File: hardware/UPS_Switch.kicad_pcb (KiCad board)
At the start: 2 copper layers, 28 parts, among them J1 Screw_Terminal_01x04, J3 Screw_Terminal_01x06, J4 Screw_Terminal_01x06, U1 ESP32-DEVKIT-V1, U2 TPS259807ONRGER, U3 TPS259807ONRGER, U4 TPS259807ONRGER

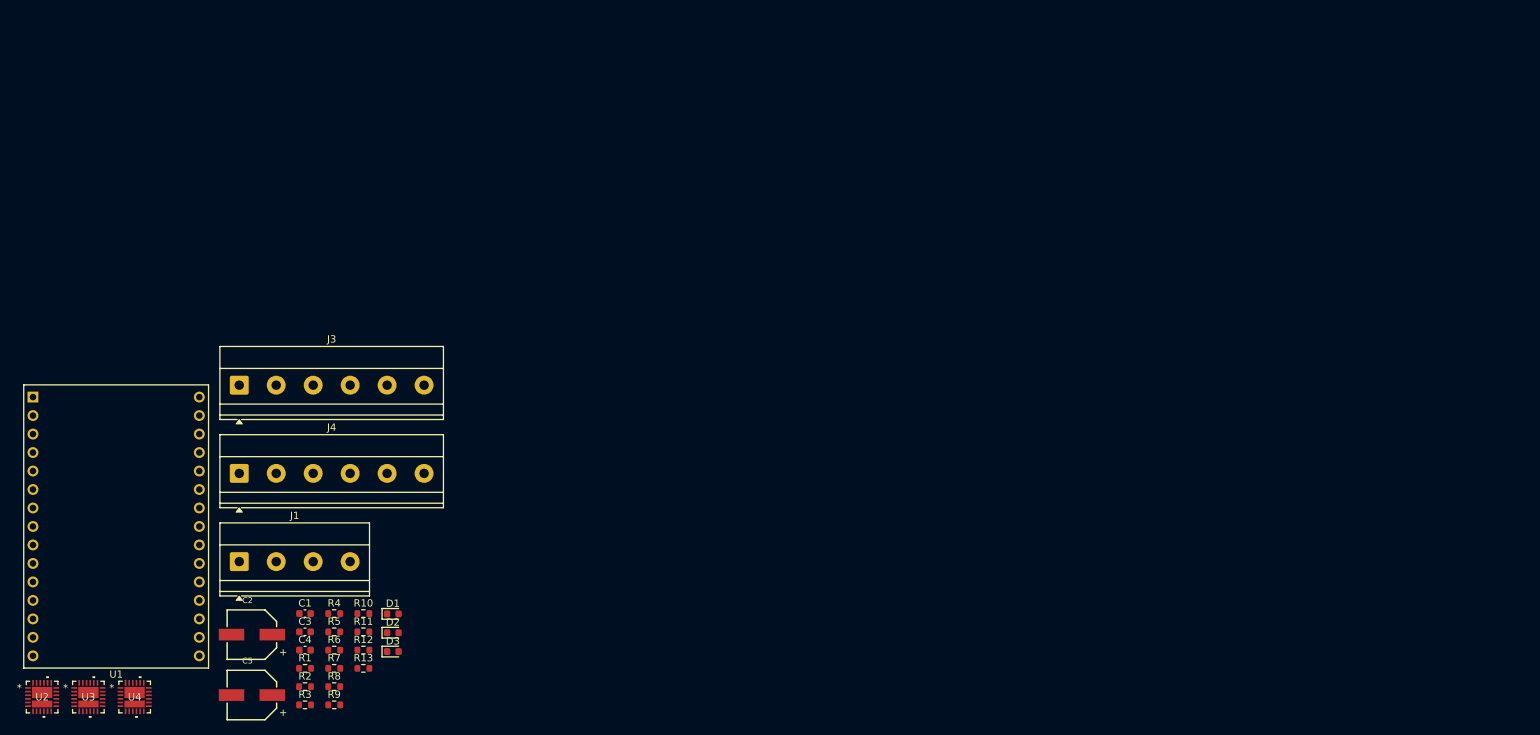
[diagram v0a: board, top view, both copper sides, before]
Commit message: layout fixes
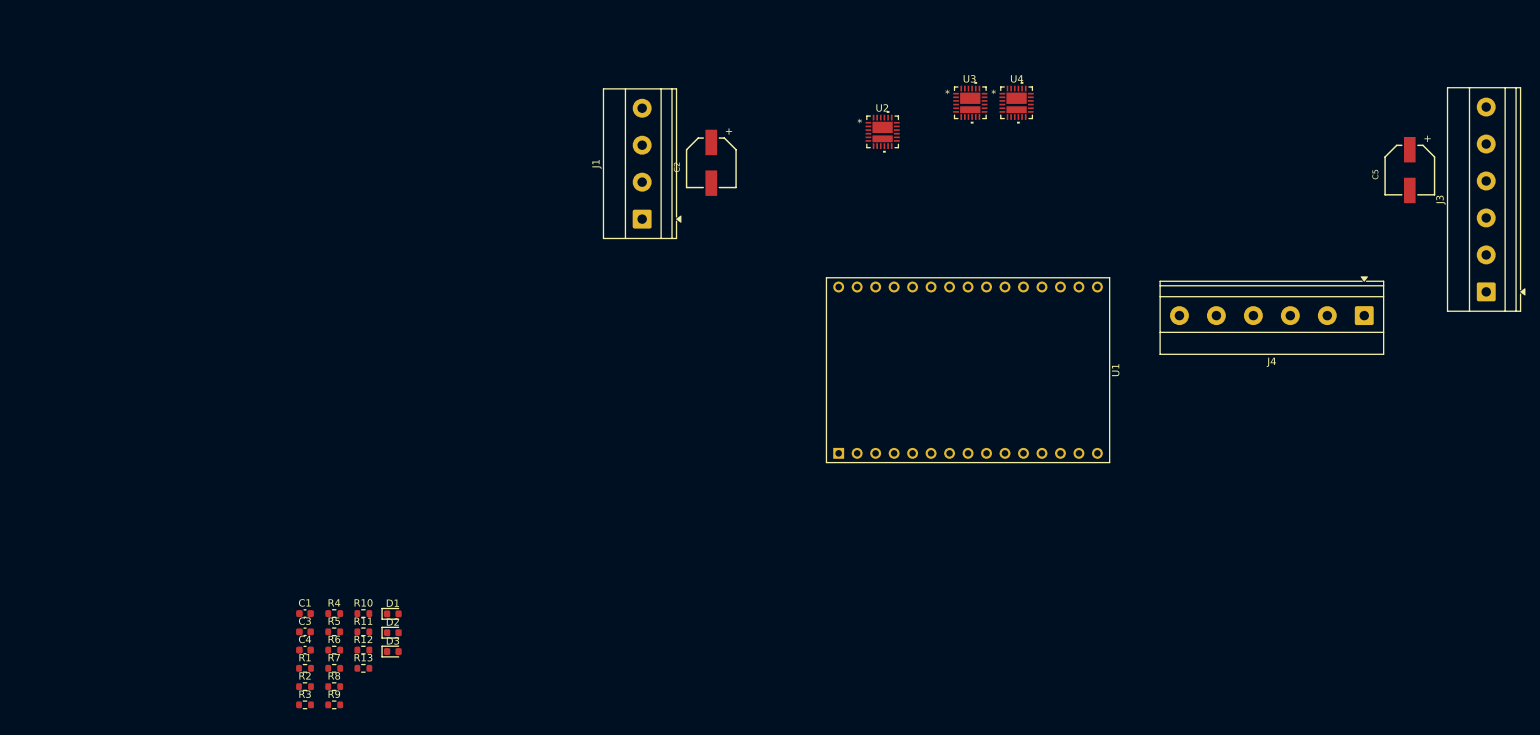
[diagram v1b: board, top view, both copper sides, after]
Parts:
- moved C5 174.7 mm to (130.0, 37.5), turned to 90 degrees
- moved J3 171.9 mm to (140.5, 54.2), turned to 90 degrees
- moved J4 156.1 mm to (123.7, 57.5), turned to 180 degrees
- moved U3 146.2 mm to (69.6, 28.2)
- moved U4 146.2 mm to (76.0, 28.2)
- moved U2 139.2 mm to (57.5, 32.2)
- moved U1 111.0 mm to (51.5, 76.4), turned to 90 degrees
- moved C2 90.5 mm to (34.0, 36.5), turned to 90 degrees
- moved J1 72.7 mm to (24.5, 44.2), turned to 90 degrees

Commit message: Updated layout and screengrabs
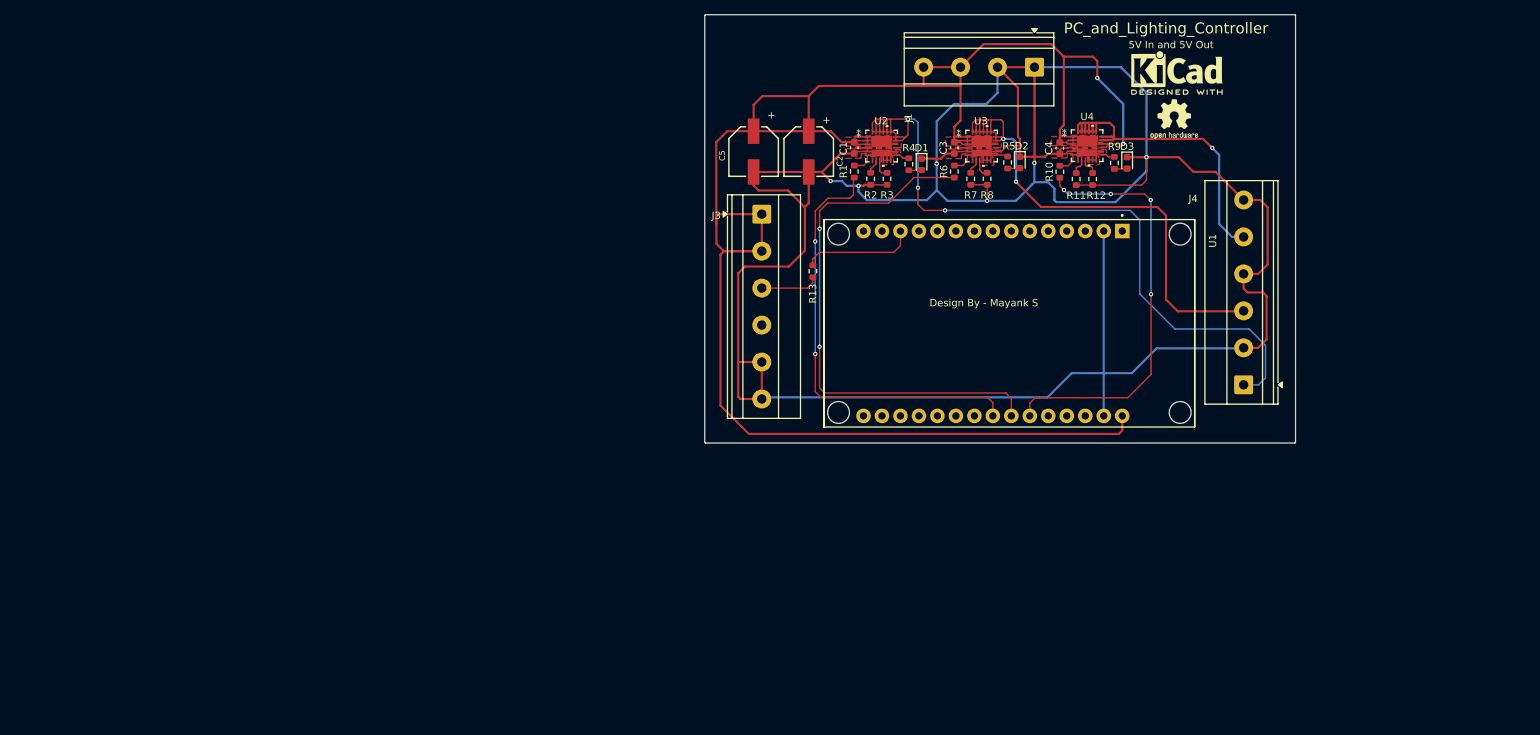
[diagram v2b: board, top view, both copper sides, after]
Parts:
- added REF**: KiCad-Logo2_5mm_SilkScreen, Symbol:KiCad-Logo2_5mm_SilkScreen, F.Cu at (98.0, 24.1)
- added REF**: OSHW-Logo2_7.3x6mm_SilkScreen, Symbol:OSHW-Logo2_7.3x6mm_SilkScreen, F.Cu at (97.6, 30.5)
- U1: footprint RF_Module:ESP32-C3-DevKitM-1 -> Footprints:MODULE_ESP32_DEVKIT_V1
- moved R9 130.6 mm to (89.4, 36.5), turned to 90 degrees
- moved C4 124.6 mm to (81.9, 34.5), turned to -90 degrees
- moved D3 121.2 mm to (91.2, 36.5), turned to -90 degrees
- moved R12 119.3 mm to (86.4, 38.7), turned to -90 degrees
- moved R11 116.1 mm to (84.2, 38.7), turned to -90 degrees
- moved R8 113.7 mm to (71.9, 38.7), turned to -90 degrees
- moved R10 113.3 mm to (81.9, 37.7), turned to 90 degrees
- moved R5 112.8 mm to (74.7, 36.4), turned to 90 degrees
- moved C3 111.3 mm to (67.4, 34.4), turned to -90 degrees
- moved R7 110.4 mm to (69.7, 38.7), turned to -90 degrees
- moved R3 107.8 mm to (58.1, 38.7), turned to -90 degrees
- moved D2 107.7 mm to (76.4, 36.4), turned to -90 degrees
- moved R6 107.7 mm to (67.4, 37.7), turned to 90 degrees
- moved R2 104.5 mm to (55.9, 38.7), turned to -90 degrees
- moved R1 101.8 mm to (53.6, 37.7), turned to 90 degrees
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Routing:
- net GND: track 0.00 -> 454.6 mm, vias 0 -> 6
- net +5V: track 0.00 -> 290.6 mm, vias 0 -> 2
- net /LED_1_VOUT: track 0.00 -> 107.3 mm, vias 0 -> 3
- net /LED_2_VOUT: track 0.00 -> 75.6 mm, vias 0 -> 2
- net /LED_2_CTRL: track 0.00 -> 74.1 mm, vias 0 -> 2
- net /LED_1_CTRL: track 0.00 -> 60.3 mm, vias 0 -> 2
- net /LED_3_CTRL: track 0.00 -> 58.4 mm, vias 0 -> 4
- net /LED_3_VOUT: track 0.00 -> 49.0 mm, vias 0 -> 1
- net Net-(U1-TX0): track 0.00 -> 15.7 mm
- net /Motor_PWM: track 0.00 -> 8.09 mm
- net /LED_3_EN: track 0.00 -> 2.92 mm
- net /LED_1_EN: track 0.00 -> 2.91 mm
- net /LED_2_EN: track 0.00 -> 2.85 mm
- net /LED3_IMON: track 0.00 -> 2.58 mm
- net /LED1_IMON: track 0.00 -> 2.57 mm
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- added copper zone on F.Cu, net +5V
- added copper zone on F.Cu, net GND
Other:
- board outline added: 81.2 x 58.9 mm
- board text added: "5V In and 5V Out"
- board text added: "Design By - Mayank S"
- board text added: "PC_and_Lighting_Controller"
